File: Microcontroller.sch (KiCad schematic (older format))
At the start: 15 parts, among them J1 USB, P23 CONN_1, U3 PIC18F4550, X1 4MHz

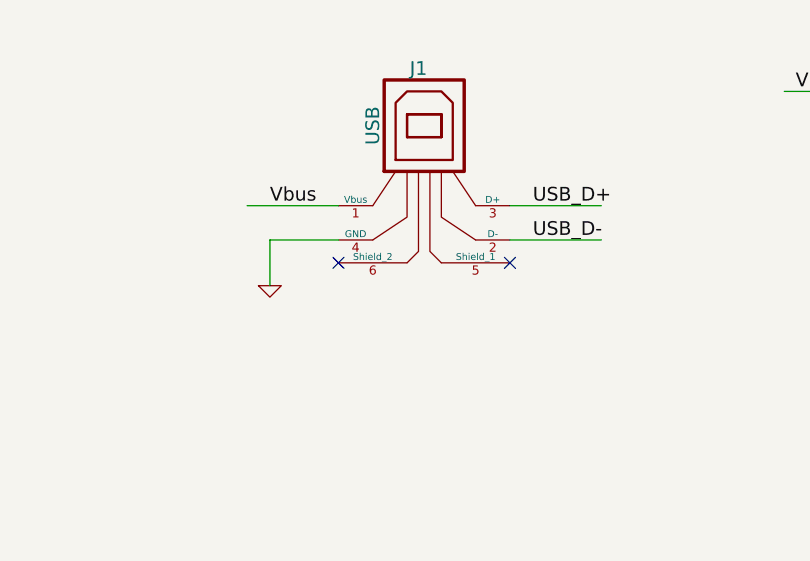
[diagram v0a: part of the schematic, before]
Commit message: Changed the footprint of the PIC to the correct one. Changed the layout of the development area, to be more suited for development Changed the layout of the reset button and programmer header. The programmer header now needs to be a 90deg header, for the pickit3 to fit Added components for the mounting holes and OSHW logos.
Signed-off-by: Kolijn Wolfaardt <kolijn.wolfaardt2gmail.com>
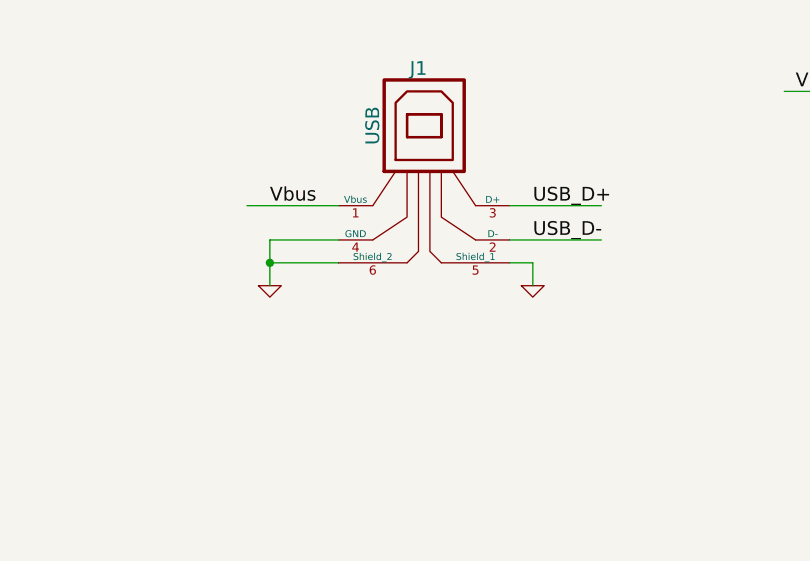
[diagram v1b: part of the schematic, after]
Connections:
- wire segments 118 -> 121
- no-connect marks 3 -> 1
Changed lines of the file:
@@
 LIBS:pic18f4550
 LIBS:l293
-LIBS:dp_devices
 LIBS:Robotics Board-cache
 EELAYER 27 0
@@
 Sheet 4 6
 Title ""
-Date "12 feb 2014"
+Date "18 apr 2014"
 Rev ""
 Comp ""
@@
 Wire Wire Line
 	6300 1750 6700 1750
-NoConn ~ 6300 1850
-NoConn ~ 5550 1850
 Wire Wire Line
 	3350 1200 3850 1200
@@
 	2350 3750 2250 3750
 Connection ~ 2250 3750
+Wire Wire Line
+	5550 1850 5250 1850
+Connection ~ 5250 1850
+$Comp
+L GND #PWR038
+U 1 1 53514222
+P 6400 1950
+F 0 "#PWR038" H 6400 1950 30  0001 C CNN
+F 1 "GND" H 6400 1880 30  0001 C CNN
+F 2 "" H 6400 1950 60  0000 C CNN
+F 3 "" H 6400 1950 60  0000 C CNN
+	1    6400 1950
+	1    0    0    -1
+$EndComp
+Wire Wire Line
+	6300 1850 6400 1850
+Wire Wire Line
+	6400 1850 6400 1950
 $EndSCHEMATC

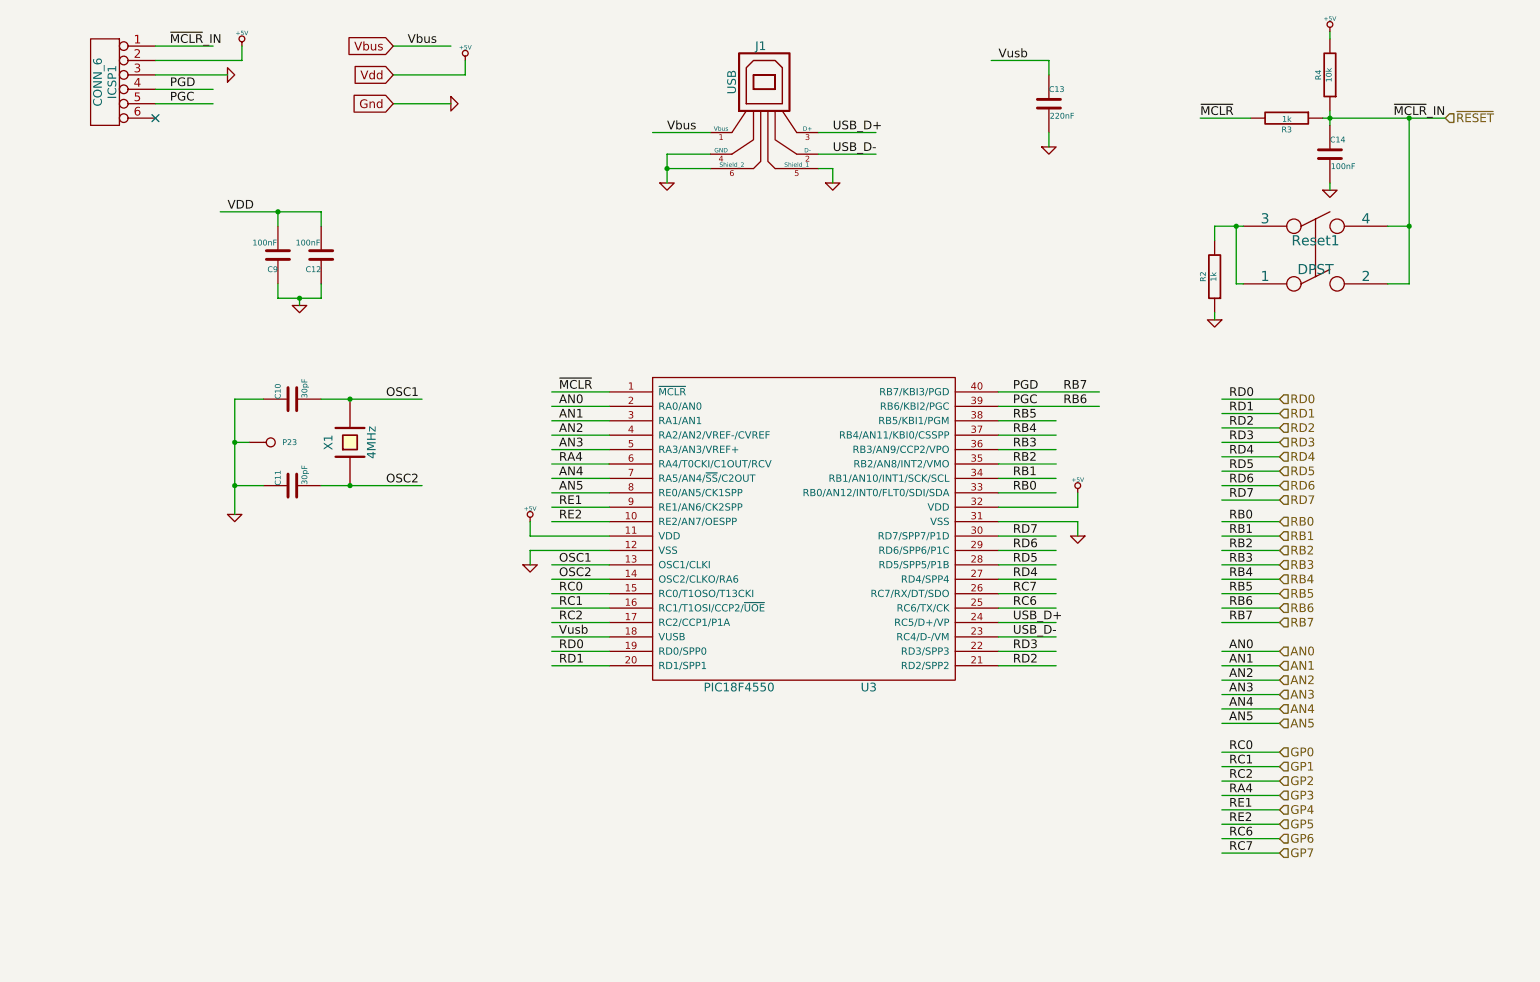
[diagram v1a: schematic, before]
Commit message: Changed to FTDI chip, cut space from development area
An FTDI chip was added to provide the USB communications rather than the PIC
A jumper is available to choose if the USB datalines go to the FTDI chip or the
PIC.

The development area was reduced to provide space for the FTDI chip.

Signed-off-by: Kolijn Wolfaardt <kolijn.wolfaardt@gmail.com>
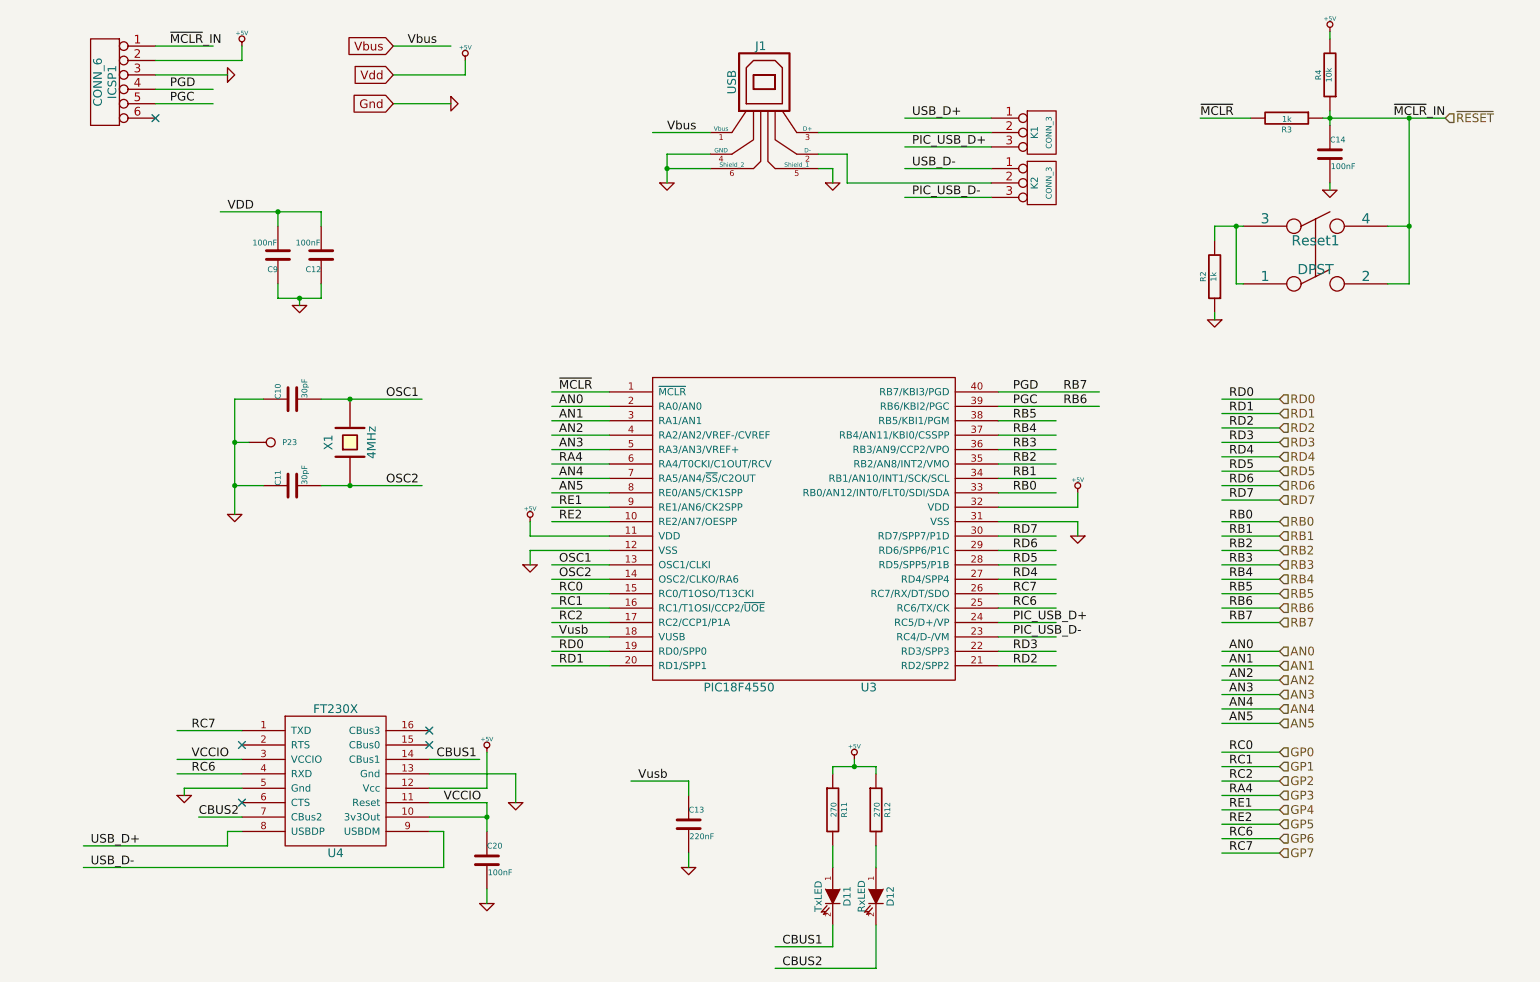
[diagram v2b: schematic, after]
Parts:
- added C20: 100nF, ~, symbol C
- added D11: TxLED, ~, symbol LED
- added D12: RxLED, ~, symbol LED
- added K1, K2: CONN_3, symbol CONN_3
- added R11, R12: 270, ~, symbol R
- added U4: FT230X, ~, symbol FT230X
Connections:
- net labels added: CBUS1, CBUS2, PIC_USB_D+, PIC_USB_D-, VCCIO
- wire segments 121 -> 158
- no-connect marks 1 -> 5
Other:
- moved on the sheet: C13

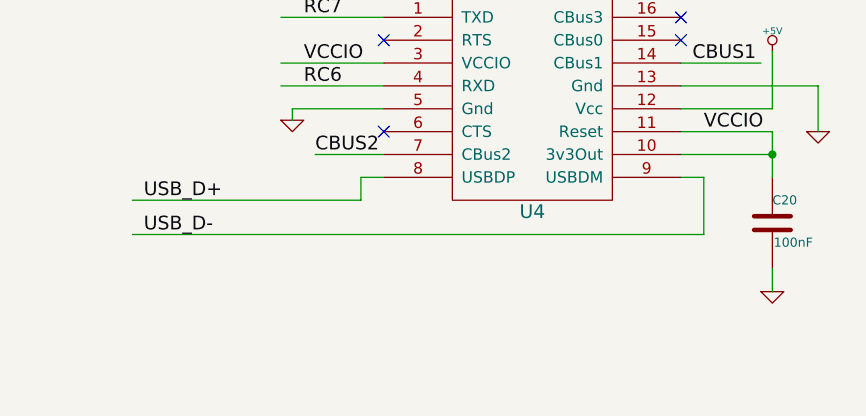
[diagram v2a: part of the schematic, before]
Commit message: Eddited USB circuit to include resistors and capacitors.
Signed-off-by: Kolijn Wolfaardt <kolijn.wolfaardt@gmail.com>
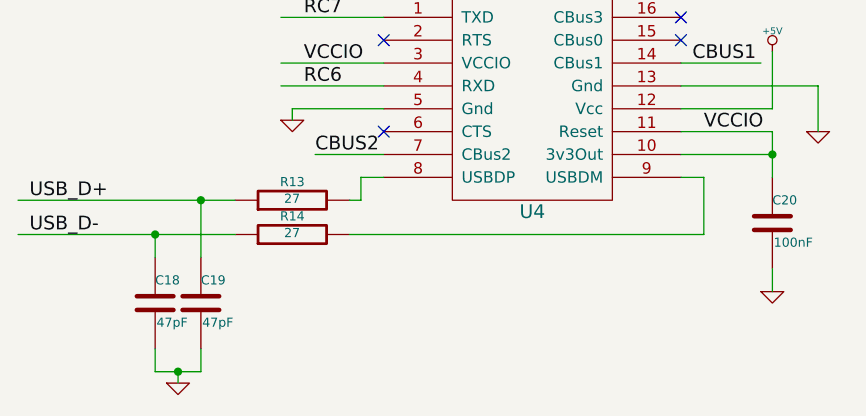
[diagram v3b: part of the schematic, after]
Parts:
- added C18, C19: 47pF, ~, symbol C
- added R13, R14: 27, ~, symbol R
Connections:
- wire segments 158 -> 166
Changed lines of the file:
@@
 	1    0    0    -1
 $EndComp
-Text Label 1250 6550 0    60   ~ 0
+Text Label 750  6550 0    60   ~ 0
 USB_D+
-Text Label 1250 6700 0    60   ~ 0
+Text Label 750  6700 0    60   ~ 0
 USB_D-
 Wire Wire Line
@@
 	6400 1850 6400 1950
 Wire Wire Line
-	1200 6550 2200 6550
-Wire Wire Line
-	1200 6700 3700 6700
+	700  6550 1650 6550
 Wire Wire Line
 	2200 6550 2200 6450
@@
 	6700 6000 6700 6050
 Connection ~ 6550 6000
+Wire Wire Line
+	700  6700 1650 6700
+$Comp
+L C C18
+U 1 1 535267EE
+P 1300 7000
+F 0 "C18" H 1300 7100 40  0000 L CNN
+F 1 "47pF" H 1306 6915 40  0000 L CNN
+F 2 "~" H 1338 6850 30  0000 C CNN
+F 3 "~" H 1300 7000 60  0000 C CNN
+	1    1300 7000
+	1    0    0    -1
+$EndComp
+$Comp
+L C C19
+U 1 1 535267FB
+P 1500 7000
+F 0 "C19" H 1500 7100 40  0000 L CNN
+F 1 "47pF" H 1506 6915 40  0000 L CNN
+F 2 "~" H 1538 6850 30  0000 C CNN
+F 3 "~" H 1500 7000 60  0000 C CNN
+	1    1500 7000
+	1    0    0    -1
+$EndComp
+$Comp
+L R R13
+U 1 1 53526803
+P 1900 6550
+F 0 "R13" V 1980 6550 40  0000 C CNN
+F 1 "27" V 1907 6551 40  0000 C CNN
+F 2 "~" V 1830 6550 30  0000 C CNN
+F 3 "~" H 1900 6550 30  0000 C CNN
+	1    1900 6550
+	0    -1   -1   0
+$EndComp
+$Comp
+L R R14
+U 1 1 53526810
+P 1900 6700
+F 0 "R14" V 1980 6700 40  0000 C CNN
+F 1 "27" V 1907 6701 40  0000 C CNN
+F 2 "~" V 1830 6700 30  0000 C CNN
+F 3 "~" H 1900 6700 30  0000 C CNN
+	1    1900 6700
+	0    -1   -1   0
+$EndComp
+$Comp
+L GND #PWR044
+U 1 1 53526826
+P 1400 7350
+F 0 "#PWR044" H 1400 7350 30  0001 C CNN
+F 1 "GND" H 1400 7280 30  0001 C CNN
+F 2 "" H 1400 7350 60  0000 C CNN
+F 3 "" H 1400 7350 60  0000 C CNN
+	1    1400 7350
+	1    0    0    -1
+$EndComp
+Wire Wire Line
+	1400 7350 1400 7300
+Wire Wire Line
+	1300 7300 1500 7300
+Wire Wire Line
+	1500 7300 1500 7200
+Wire Wire Line
+	1300 7300 1300 7200
+Connection ~ 1400 7300
+Wire Wire Line
+	1300 6700 1300 6800
+Connection ~ 1300 6700
+Wire Wire Line
+	1500 6550 1500 6800
+Connection ~ 1500 6550
+Wire Wire Line
+	2150 6550 2200 6550
+Wire Wire Line
+	2150 6700 3700 6700
 $EndSCHEMATC

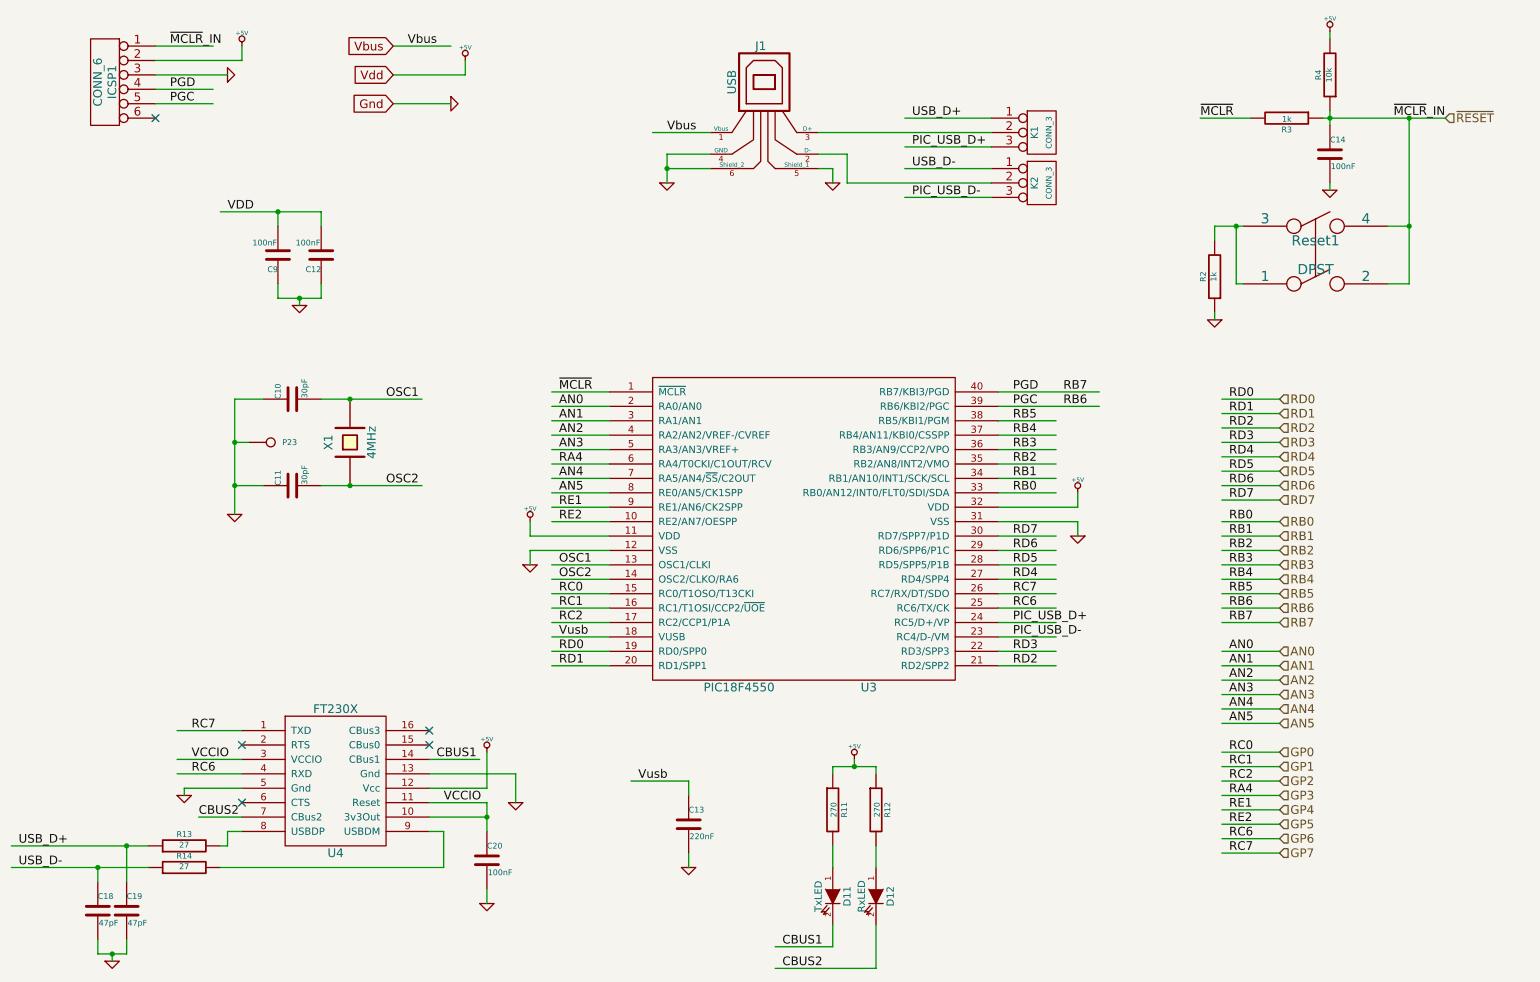
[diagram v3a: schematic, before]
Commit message: Changed the board to use 3.3v rather than 5v. Total new layout.
Since the FTDI chip cannot communicate with the 5v PIC. So run
the PIC at 3.3v This limits the maximum crystal frequency of
the pic, but 4MHz is fine. the internal usb regulator is no
longer used and is replaced with the external one.

The 3.3v regulator get it's 5v from the selected 5v source.
5v is still used by the FTDI chip and the Motor driver.

Signed-off-by: Kolijn Wolfaardt <kolijn.wolfaardt@gmail.com>
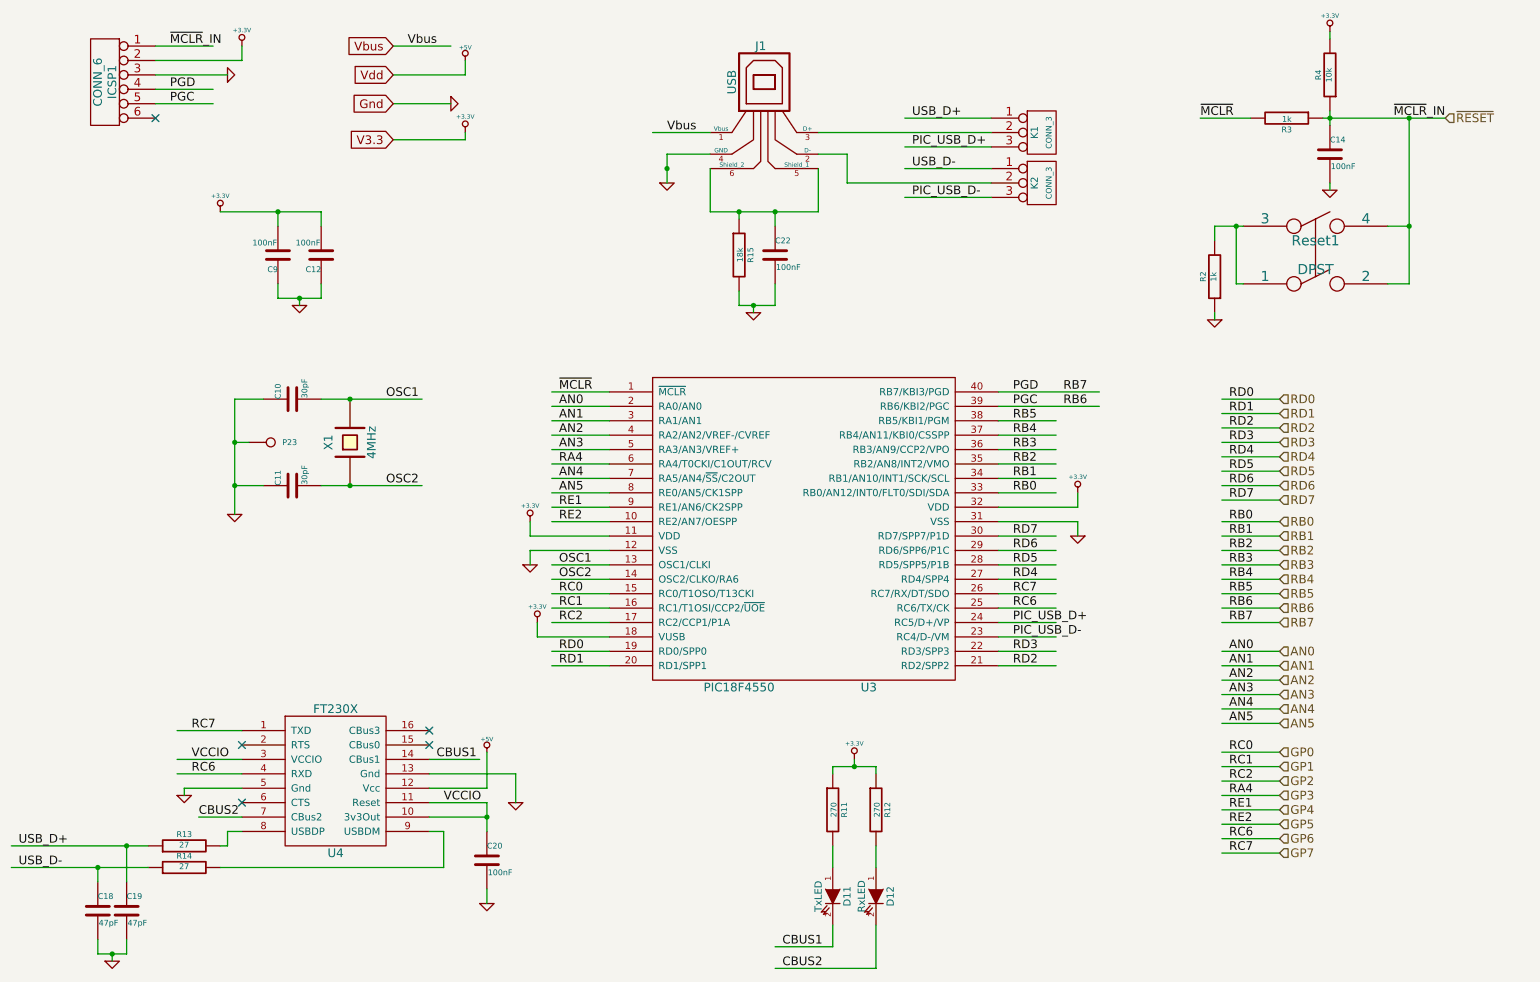
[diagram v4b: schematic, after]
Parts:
- removed C13: 220nF, ~, symbol C
- added C22: 100nF, ~, symbol C
- added R15: 18k, ~, symbol R
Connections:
- net labels added: +3.3V, V3.3
- net labels removed: VDD, Vusb
- wire segments 166 -> 172
